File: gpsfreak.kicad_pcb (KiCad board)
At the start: 4 copper layers, 79.8 x 47.2 mm, 157 parts, among them J10 Skedd, J13 Boot, J2 SMA, J3 SMA, J4 SMA, J5 U.Fl, J6 SMA, J7 USB_C_Receptacle_16P, J8 U.Fl, J9 U.Fl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

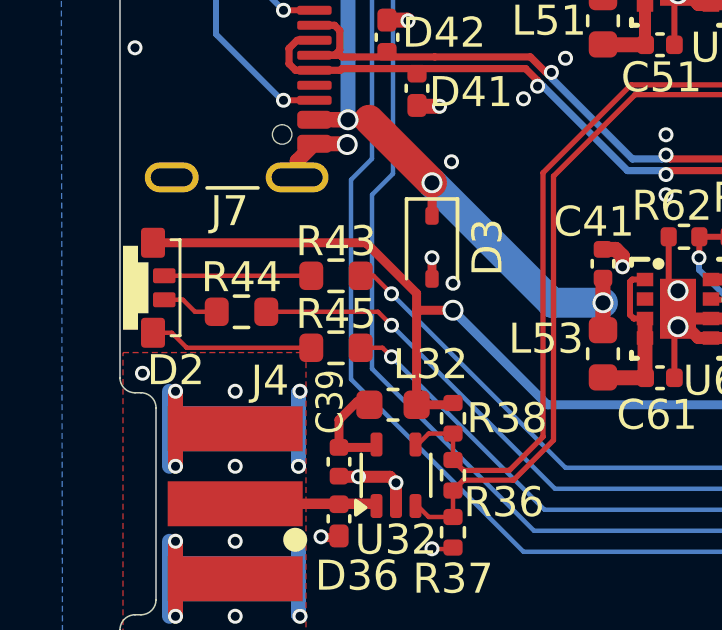
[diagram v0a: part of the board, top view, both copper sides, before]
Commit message: Instead, switch to a RGB LED footprint from Paul Elliot.
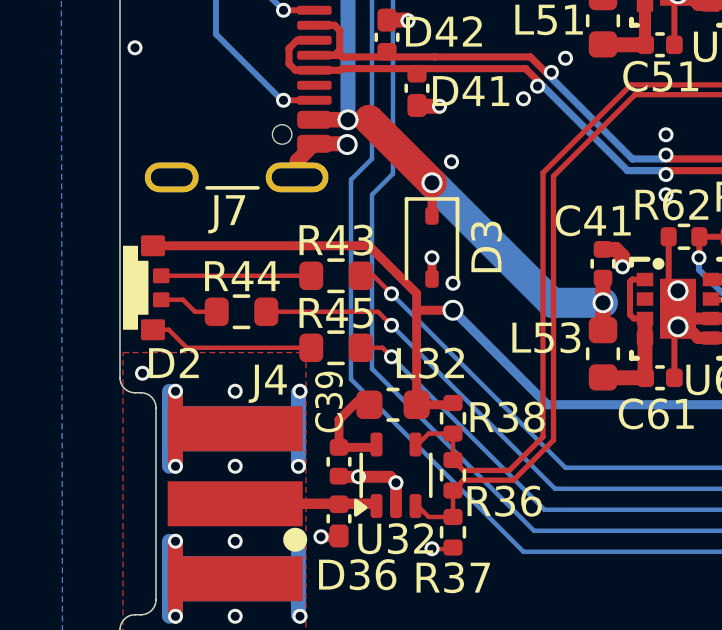
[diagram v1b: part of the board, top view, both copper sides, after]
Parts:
- D2: footprint Parts:LED-QPLB615-RGB -> Parts:LED_RGB_SIDE
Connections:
- D2 pad 1: Net-(D2-GK) -> +3V3
- D2 pad 3: +3V3 -> Net-(D2-A)
- R44 pad 1: Net-(D2-GK) -> Net-(D2-A)
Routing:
- net Net-(D2-A): track 0.00 -> 2.02 mm
- net Net-(D2-GK): track 1.92 -> 0.00 mm

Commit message: Split each output onto it's own sheet.
Makes it easier to mix'n'match output types for board spins.
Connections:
- net /Outputs/Ext2 renamed /Output2/Ext2
- net /Outputs/Ext3 renamed /Output3/Ext3
- net /Outputs/Ext4 renamed /Output4/Ext3
- net OUT1_N renamed /OUT1_N
- net OUT1_P renamed /OUT1_P
- net OUT2_N renamed /OUT2_N
- net OUT2_P renamed /OUT2_P
- net OUT3_N renamed /OUT3_N
- net OUT3_P renamed /OUT3_P
- net OUT4_N renamed /OUT4_N
- net OUT4_P renamed /OUT4_P
- net OUT5 renamed /OUT5
- U2 pad 41: unconnected-(U2-OUT5_N-Pad41) -> /Clocking/OUT5_N

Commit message: Touch up net names.
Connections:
- U2 pad 38: unconnected-(U2-OUT4_N-Pad38) -> /Clocking/OUT4_N
- U2 pad 39: unconnected-(U2-OUT4_P-Pad39) -> /Clocking/OUT4_P
